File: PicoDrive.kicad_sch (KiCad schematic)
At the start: 36 parts, among them J1 Conn_01x02, J8 Conn_02x05_Odd_Even, J9 Conn_01x05, Q1 PSMN4R5-30YLC, U1 rp2040-zero, U6 TCA9554DB, U7 TCA9554DB, U8 LTC4357MS8, U9 INA219BIDR

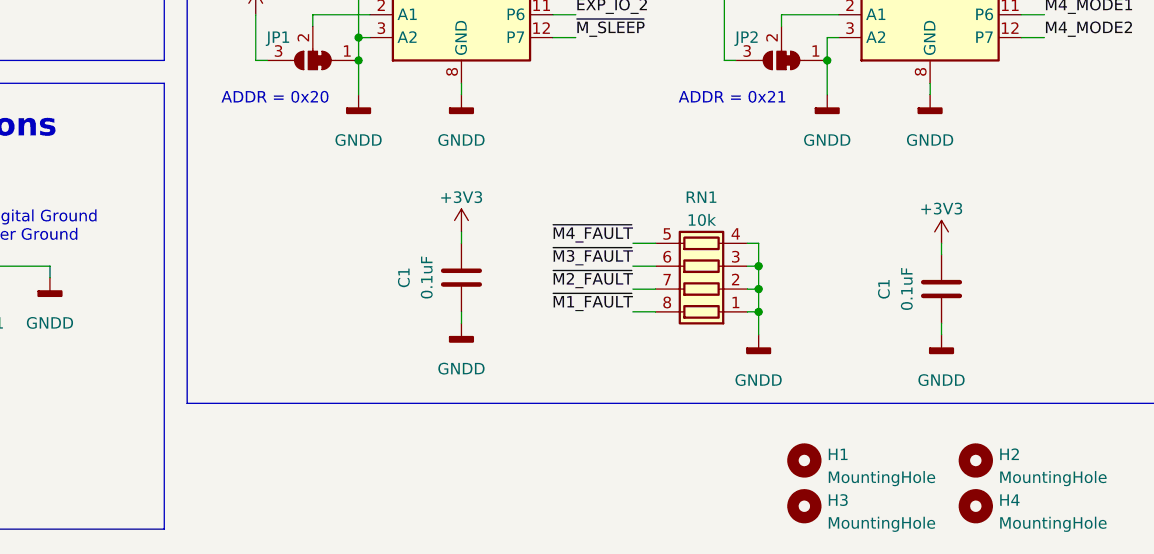
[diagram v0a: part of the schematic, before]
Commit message: Add mouser no's, pullup resistor, change project name
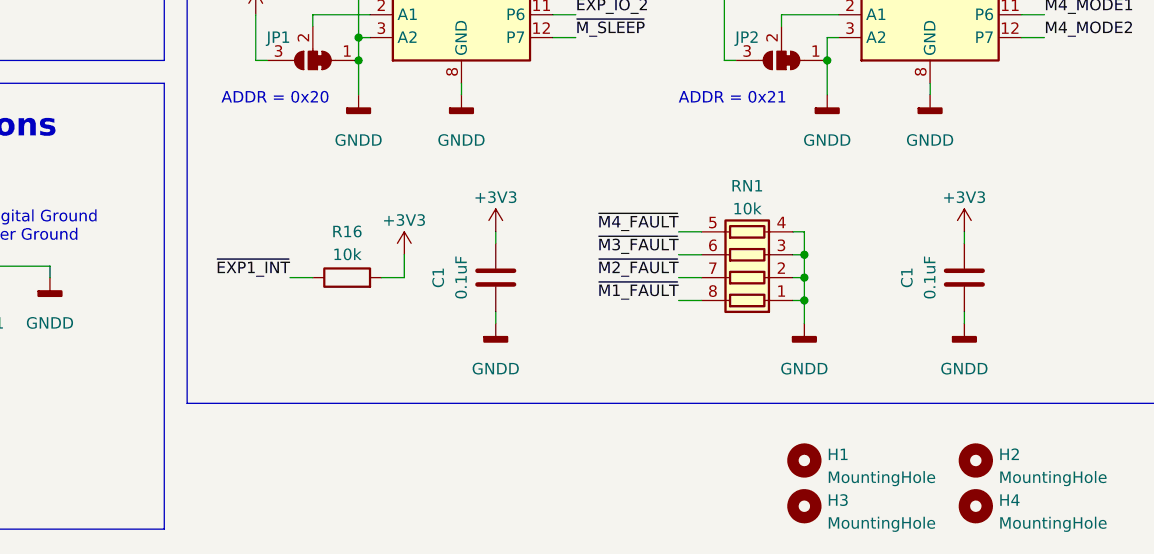
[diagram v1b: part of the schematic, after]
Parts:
- added R16: 10k, Resistor_SMD:R_0805_2012Metric_Pad1.20x1.40mm_HandSolder, symbol Device:R
- C1: Mouser No (none) -> 581-08055C104J
- C3: Mouser No (none) -> 647-UVZ1J101MPD
- J1: Mouser No (none) -> 490-TB009-508-02BE
- J8: Mouser No (none) -> 710-61201021621
- PS1: MANUFACTURER CUI Inc -> (none); Mouser No (none) -> 490-P78E03-1000; STANDARD Manufacturer Recommendations -> (none)
- Q1: Mouser No (none) -> 771-PSMN4R5-30YLC115
- R1: Mouser No (none) -> 504-MSMA2512R0050FEN
- R11: Mouser No (none) -> 71-RCC0805100RFKEA
- R13, R14: Mouser No (none) -> 71-RCC080510R0FKEA
- R15: Mouser No (none) -> 652-CRS0805FX1002ELF
- R5, R6: Mouser No (none) -> 71-CRCW0805-1.65K-E3
- RN1: Mouser No (none) -> 603-YC324-JK-0710KL
- U6, U7: Mouser No (none) -> 595-TCA9554DWR
- U8: Mouser No (none) -> 584-LTC4357CMS8#PBF
- U9: Mouser No (none) -> 595-INA219BIDR
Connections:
- net +3V3: now also R16.2
- net ~{EXP1_INT}: now also R16.1
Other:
- moved on the sheet: C1, RN1

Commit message: Fix io expander component to match footprint
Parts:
- U6, U7: Mfr. No TCA9554DWR -> TCA9554DBR; Mouser No 595-TCA9554DWR -> 595-TCA9554DBR
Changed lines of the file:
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@@
       (effects (font (size 1.27 1.27)) hide)
     )
-    (property "Mfr. No" "TCA9554DWR" (at 203.2 97.79 0)
-      (effects (font (size 1.27 1.27)) hide)
-    )
-    (property "Mouser No" "595-TCA9554DWR" (at 203.2 97.79 0)
+    (property "Mfr. No" "TCA9554DBR" (at 203.2 97.79 0)
+      (effects (font (size 1.27 1.27)) hide)
+    )
+    (property "Mouser No" "595-TCA9554DBR" (at 203.2 97.79 0)
       (effects (font (size 1.27 1.27)) hide)
     )
@@
       (effects (font (size 1.27 1.27)) hide)
     )
-    (property "Mfr. No" "TCA9554DWR" (at 255.27 97.79 0)
-      (effects (font (size 1.27 1.27)) hide)
-    )
-    (property "Mouser No" "595-TCA9554DWR" (at 255.27 97.79 0)
-      (effects (font (size 1.27 1.27)) hide)
-    )
+    (property "Mfr. No" "TCA9554DBR" (at 255.27 97.79 0)
+      (effects (font (size 1.27 1.27)) hide)
+    )
+    (property "Mouser No" "595-TCA9554DBR" (at 255.27 97.79 0)
+      (effects (font (size 1.27 1.27)) hide)
+    )

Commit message: Fix mfault pullup resistor (it was configured as a pulldown)
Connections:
- net +3V3: now also RN1.1 (R1.1), RN1.2 (R2.1), RN1.3 (R3.1), RN1.4 (R4.1)
- net GND1: no longer RN1.1 (R1.1), RN1.2 (R2.1), RN1.3 (R3.1), RN1.4 (R4.1)
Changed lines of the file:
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@@
   (junction (at 232.41 102.87) (diameter 0) (color 0 0 0 0)
   )
-  (junction (at 241.3 137.16) (diameter 0) (color 0 0 0 0)
-  )
   (junction (at 154.94 53.34) (diameter 0) (color 0 0 0 0)
   )
@@
   (junction (at 80.01 40.64) (diameter 0) (color 0 0 0 0)
   )
+  (junction (at 241.3 129.54) (diameter 0) (color 0 0 0 0)
+  )
   (junction (at 53.34 71.12) (diameter 0) (color 0 0 0 0)
   )
@@
     (stroke (width 0) (type default))
   )
-  (wire (pts (xy 241.3 137.16) (xy 241.3 139.7))
-    (stroke (width 0) (type default))
-  )
   (wire (pts (xy 93.98 144.78) (xy 93.98 146.05))
     (stroke (width 0) (type default))
@@
   )
   (wire (pts (xy 203.2 113.03) (xy 203.2 114.3))
+    (stroke (width 0) (type default))
+  )
+  (wire (pts (xy 241.3 128.27) (xy 241.3 129.54))
     (stroke (width 0) (type default))
   )
@@
     )
   )
+  (symbol (lib_id "power:+3V3") (at 241.3 128.27 0) (unit 1)
+    (in_bom yes) (on_board yes) (dnp no) (fields_autoplaced)
+    (property "Reference" "#PWR064" (at 241.3 132.08 0)
+      (effects (font (size 1.27 1.27)) hide)
+    )
+    (property "Value" "+3V3" (at 241.3 124.46 0)
+      (effects (font (size 1.27 1.27)))
+    )
+    (property "Footprint" "" (at 241.3 128.27 0)
+      (effects (font (size 1.27 1.27)) hide)
+    )
+    (property "Datasheet" "" (at 241.3 128.27 0)
+      (effects (font (size 1.27 1.27)) hide)
+    )
+    (pin "1")
+    (instances
+      (project "PicoDrive"
+        (path "/738c766b-5149-4d22-8944-003aead1c6f2"
+          (reference "#PWR064") (unit 1)
+        )
+      )
+    )
+  )
   (symbol (lib_id "Sensor_Energy:INA219BxD") (at 55.88 140.97 0) (unit 1)
     (in_bom yes) (on_board yes) (dnp no) (fields_autoplaced)
@@
         )
       )
-    )
-  )
-  (symbol (lib_id "power:GNDD") (at 241.3 139.7 0) (unit 1)
-    (in_bom yes) (on_board yes) (dnp no) (fields_autoplaced)
-    (property "Reference" "#PWR036" (at 241.3 146.05 0)
-      (effects (font (size 1.27 1.27)) hide)
-    )
-    (property "Value" "GNDD" (at 241.3 144.78 0)
-      (effects (font (size 1.27 1.27)))
-    )
-    (property "Footprint" "" (at 241.3 139.7 0)
-      (effects (font (size 1.27 1.27)) hide)
-    )
-    (property "Datasheet" "" (at 241.3 139.7 0)
-      (effects (font (size 1.27 1.27)) hide)
-    )
-    (pin "1")
-    (instances
-      (project "PicoDrive"
-        (path "/738c766b-5149-4d22-8944-003aead1c6f2"
-          (reference "#PWR036") (unit 1)
-        )
-      )
